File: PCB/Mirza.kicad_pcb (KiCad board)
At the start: 2 copper layers, 74 x 34 mm, 99 parts, among them J1 In, J2 Out, J3 Power, Q1 PMP5201Y, Q10 PMP5201Y, Q11 PMP4201Y, Q12 PMP4201Y, Q13 2SC3324, Q14 2SA1312, Q15 2SA1312, Q16 2SA1312, Q17 2SC3324, Q18 2SC3324, Q19 PMP4201Y, Q2 PMP4201Y, Q20 PMP5201Y, Q21 PMP4201Y, Q22 2SA1312, Q23 2SC3324, Q24 2SC3324, Q25 2SA1312, Q26 D45H11, Q27 D44H11, Q28 PMP5201Y, Q3 2SA1312, Q4 2SC3324, Q5 2SC3324, Q6 2SC3324, Q7 2SA1312, Q8 2SA1312, Q9 PMP5201Y, U1 OPA604

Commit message: Initial public upload
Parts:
- added H3: JLC Tooling Hole, Ariamelon-HolePad:MountingHole_JLC-Tooling, F.Cu at (67.0, 83.0)
- added H4: JLC Tooling Hole, Ariamelon-HolePad:MountingHole_JLC-Tooling, F.Cu at (67.0, 52.0)
- added H5: JLC Tooling Hole, Ariamelon-HolePad:MountingHole_JLC-Tooling, F.Cu at (129.5, 80.0)
- added H6: JLC Tooling Hole, Ariamelon-HolePad:MountingHole_JLC-Tooling, F.Cu at (129.5, 55.0)
- added R32: 1, Resistor_SMD:R_MiniMELF_MMA-0204, F.Cu at (114.8, 61.4)
- added R33: 1, Resistor_SMD:R_MiniMELF_MMA-0204, F.Cu at (114.8, 73.6)
- added R34: 1, Resistor_SMD:R_MiniMELF_MMA-0204, F.Cu at (117.2, 61.4)
- added R35: 1, Resistor_SMD:R_MiniMELF_MMA-0204, F.Cu at (117.2, 73.6)
- C14: renamed from C10; value 1u -> 100n
- C15: renamed from C11; value 1u -> 100n
- C16: renamed from C12; footprint Capacitor_THT:CP_Radial_D6.3mm_P2.50mm -> Ariamelon-Device:CP_Radial_D6.3mm_P2.50mm
- C17: renamed from C13; footprint Capacitor_THT:CP_Radial_D6.3mm_P2.50mm -> Ariamelon-Device:CP_Radial_D6.3mm_P2.50mm
- C18: renamed from C14; footprint Capacitor_THT:CP_Radial_D6.3mm_P2.50mm -> Ariamelon-Device:CP_Radial_D6.3mm_P2.50mm
- C19: renamed from C15; footprint Capacitor_THT:CP_Radial_D6.3mm_P2.50mm -> Ariamelon-Device:CP_Radial_D6.3mm_P2.50mm
- C6: renamed from C19; footprint Capacitor_THT:CP_Radial_D6.3mm_P2.50mm -> Ariamelon-Device:CP_Radial_D6.3mm_P2.50mm
- C7: renamed from C21; footprint Capacitor_THT:CP_Radial_D6.3mm_P2.50mm -> Ariamelon-Device:CP_Radial_D6.3mm_P2.50mm
- C8: renamed from C20; footprint Capacitor_THT:CP_Radial_D6.3mm_P2.50mm -> Ariamelon-Device:CP_Radial_D6.3mm_P2.50mm
- C9: renamed from C18; footprint Capacitor_THT:CP_Radial_D6.3mm_P2.50mm -> Ariamelon-Device:CP_Radial_D6.3mm_P2.50mm
- H1, H2: footprint MountingHole:MountingHole_3.2mm_M3_Pad -> Ariamelon-HolePad:MountingHole_3.2mm_M3_Pad
- Q1, Q10, Q9: value PMP5201Y -> BCM857BS
- Q11, Q19, Q2: value PMP4201Y -> BCM847BS
- Q12: value PMP4201Y -> BCM847BS; footprint Package_TO_SOT_SMD:SOT-363_SC-70-6 -> Ariamelon-Package:SOT-363_SC-70-6
- Q20: renamed from Q28; value PMP5201Y -> BCM857BS
- Q21: renamed from Q20; value PMP5201Y -> BCM857BS
- Q22: renamed from Q21; value PMP4201Y -> BCM847BS
- R11, R14: value 560 -> 220
- R17, R21: value 220 -> 150
- R19, R22, R3, R4: value 100k -> 10k
- R23: renamed from R39; value 100k -> 10k
- R25: renamed from R24; value 100k -> 10k
- R36: renamed from R31; value 0R33 -> 1; footprint Resistor_SMD:R_MELF_MMB-0207 -> Resistor_SMD:R_MiniMELF_MMA-0204
- R37: renamed from R32; value 0R33 -> 1; footprint Resistor_SMD:R_MELF_MMB-0207 -> Resistor_SMD:R_MiniMELF_MMA-0204
- R38: renamed from R33; value 68 -> 150
- R41: renamed from R38; value 100k -> 10k
- U1: value OPA604 -> ADA4522-1
- moved R36 4.55 mm to (119.6, 61.4), turned to -90 degrees
- moved R37 4.55 mm to (119.6, 73.6), turned to -90 degrees
- moved Q7 0.51 mm to (75.7, 79.7), turned to 180 degrees
- moved C13 0.50 mm to (126.6, 67.5), turned to 0 degrees
- moved C16 0.50 mm to (124.3, 61.5)
- moved C17 0.50 mm to (124.3, 71.0)
- moved C18 0.50 mm to (131.3, 61.5)
- moved C19 0.50 mm to (131.3, 71.0)
- moved Q19 0.50 mm to (101.7, 52.6), turned to 180 degrees
- moved Q20 0.50 mm to (101.7, 82.3), turned to 180 degrees
- moved Q6 0.50 mm to (75.7, 55.4), turned to 180 degrees
- moved R38 0.50 mm to (122.4, 67.5), turned to 0 degrees
- moved J2 0.40 mm to (117.9, 68.8)
- moved F1 0.40 mm to (136.7, 60.4), turned to 0 degrees
- moved F2 0.40 mm to (136.7, 74.6), turned to 0 degrees
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- renumbered C6 to C10, C7 to C11, C8 to C12, C9 to C13, C16 to C20, C17 to C21, Q22 to Q23, Q23 to Q24, Q24 to Q25, Q25 to Q26, Q26 to Q27, Q27 to Q28, R23 to R24, R25 to R26, R26 to R27, R27 to R28, R28 to R29, R29 to R30, R30 to R31, R34 to R39, R35 to R40, R36 to R42, R37 to R43
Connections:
- C11 pad 1: Net-(Q20B-C2) -> Net-(Q21A-C1)
- C12 pad 1: Net-(Q25-C) (its old number) -> Net-(Q26-C)
- C12 pad 2: Net-(Q21B-C2) -> Net-(Q22A-C1)
- C13 pad 1: GND -> Net-(C13-Pad1)
- C13 pad 2: Net-(C9-Pad2) -> GND
- C14 pad 1: GND -> Net-(U1-+)
- C14 pad 2: Net-(U1-+) -> GND
- C15 pad 1: Net-(U1--) -> Net-(C15-Pad1)
- C15 pad 2: Net-(C11-Pad2) -> Net-(U1--)
- C21 pad 1: VEE -> GND
- C21 pad 2: GND -> VEE
- C3 pad 1: Net-(C3-Pad1) -> Net-(Q11A-B1)
- C3 pad 2: Net-(Q11A-B1) -> Net-(C3-Pad2)
- C5 pad 1: Net-(C3-Pad1) -> Net-(C3-Pad2)
- C7 pad 2: Net-(Q28B-B2) -> Net-(Q20A-B1)
- C9 pad 1: Net-(Q19B-B2) -> Net-(Q19A-B1)
- F1 pad 1: Net-(J3-Pin_1) -> +18V
- F1 pad 2: +18V -> Net-(J3-Pin_1)
- F2 pad 1: Net-(J3-Pin_4) -> -18V
- F2 pad 2: -18V -> Net-(J3-Pin_4)
- Q10 pad 3: Net-(Q10B-C2) -> Net-(Q10A-B1)
- Q10 pad 6: Net-(Q10A-B1) -> Net-(Q10A-C1)
- Q11 pad 3: Net-(Q11B-C2) -> Net-(Q11A-B1)
- Q11 pad 6: Net-(Q11A-B1) -> Net-(Q11A-C1)
- Q12 pad 2: Net-(Q11B-E2) -> Net-(Q11A-E1)
- Q12 pad 5: Net-(Q11B-E2) -> Net-(Q11A-E1)
- Q13 pad 2: Net-(Q10B-C2) -> Net-(Q10A-C1)
- Q14 pad 2: Net-(Q11B-C2) -> Net-(Q11A-C1)
- Q15 pad 3: Net-(Q10B-C2) -> Net-(Q10A-C1)
- Q18 pad 3: Net-(Q11B-C2) -> Net-(Q11A-C1)
- Q19 pad 1: VCC -> Net-(Q19A-E1)
- Q19 pad 4: Net-(Q19A-B1) -> VCC
- Q19 pad 5: Net-(Q19B-B2) -> Net-(Q19A-E1)
- Q20 pad 1: VEE -> Net-(Q20A-E1)
- Q20 pad 2: Net-(Q28A-B1) -> Net-(Q20A-B1)
- Q20 pad 4: Net-(Q28A-B1) -> VEE
- Q20 pad 5: Net-(Q28B-B2) -> Net-(Q20A-E1)
- Q21 pad 1: +18V -> Net-(Q21A-E1)
- Q21 pad 2: Net-(Q20A-B1) -> Net-(Q21A-B1)
- Q21 pad 3: Net-(Q20B-C2) -> Net-(Q21A-B1)
- Q21 pad 4: Net-(Q20A-B1) -> +18V
- Q21 pad 5: Net-(Q20A-C1) -> Net-(Q21A-E1)
- Q21 pad 6: Net-(Q20A-C1) -> Net-(Q21A-C1)
- Q22 pad 1: -18V -> Net-(Q22A-E1)
- Q22 pad 2: Net-(Q21A-B1) -> Net-(Q22A-B1)
- Q22 pad 3: Net-(Q21B-C2) -> Net-(Q22A-B1)
- Q22 pad 4: Net-(Q21A-B1) -> -18V
- Q22 pad 5: Net-(Q21A-C1) -> Net-(Q22A-E1)
- Q22 pad 6: Net-(Q21A-C1) -> Net-(Q22A-C1)
- Q23 pad 2: Net-(Q22-C) -> Net-(Q23-C)
- Q24 pad 2: Net-(Q23-C) -> Net-(Q24-C)
- Q24 pad 3: Net-(Q23-E) (its old number) -> Net-(Q24-E)
- Q25 pad 1: Net-(Q20B-C2) -> Net-(Q21A-C1)
- Q25 pad 3: Net-(Q23-C) -> Net-(Q24-C)
- Q26 pad 1: Net-(Q21B-C2) -> Net-(Q22A-C1)
- Q26 pad 2: Net-(Q25-C) (its old number) -> Net-(Q26-C)
- Q26 pad 3: Net-(Q22-C) -> Net-(Q23-C)
- Q27 pad 2: Net-(Q23-C) -> Net-(Q24-C)
- Q28 pad 1: Net-(Q25-C) (its old number) -> Net-(Q26-C)
- Q28 pad 2: Net-(Q22-C) -> Net-(Q23-C)
- Q9 pad 2: Net-(Q10B-E2) -> Net-(Q10A-E1)
- Q9 pad 3: Net-(Q10A-E1) -> Net-(Q10B-E2)
- Q9 pad 5: Net-(Q10B-E2) -> Net-(Q10A-E1)
- Q9 pad 6: Net-(Q10B-E2) -> Net-(Q10A-E1)
- R1 pad 1: Net-(C1-Pad2) -> Net-(J1-Pin_2)
- R1 pad 2: Net-(J1-Pin_2) -> Net-(C1-Pad2)
- R10 pad 1: Net-(Q2A-B1) -> VEE
- R10 pad 2: VEE -> Net-(Q2A-B1)
- R11 pad 1: VCC -> Net-(Q9B-E2)
- R11 pad 2: Net-(Q9B-E2) -> VCC
- R12 pad 1: Amp_FB -> Net-(Q4-C)
- R12 pad 2: Net-(Q4-C) -> Amp_FB
- R13 pad 1: Net-(Q3-C) -> Amp_FB
- R13 pad 2: Amp_FB -> Net-(Q3-C)
- R14 pad 1: Net-(Q12B-E2) -> VEE
- R14 pad 2: VEE -> Net-(Q12A-E1)
- R15 pad 1: Amp_Out -> Net-(C2-Pad2)
- R15 pad 2: Net-(C2-Pad2) -> Amp_Out
- R16 pad 1: Net-(C3-Pad1) -> Net-(C3-Pad2)
- R17 pad 1: Net-(Q9A-E1) -> VCC
- R17 pad 2: VCC -> Net-(Q9A-E1)
- R19 pad 1: Net-(Q17-B) -> Net-(Q16-B)
- R19 pad 2: Net-(Q16-B) -> Net-(Q17-B)
- R21 pad 2: Net-(Q12A-E1) -> Net-(Q12B-E2)
- R22 pad 1: +18V -> Net-(Q19A-B1)
- R22 pad 2: Net-(Q19B-B2) -> +18V
- R23 pad 1: -18V -> Net-(Q20A-B1)
- R23 pad 2: Net-(Q28B-B2) -> -18V
- R25 pad 1: Net-(Q21A-C1) -> Net-(Q21A-B1)
- R25 pad 2: Net-(Q20A-C1) -> Net-(Q22A-B1)
- R26 pad 1: Net-(R25-Pad1) -> Net-(Q21A-E1)
- R26 pad 2: Net-(Q20A-B1) -> Net-(R26-Pad2)
- R27 pad 2: Net-(Q20B-C2) -> Net-(Q21A-C1)
- R28 pad 1: Net-(Q21B-C2) -> Net-(Q24-E)
- R28 pad 2: Net-(Q23-E) (its old number) -> Net-(Q22A-C1)
- R29 pad 1: Net-(Q21A-B1) -> Net-(Q22A-E1)
- R31 pad 1: -18V -> Net-(Q26-C)
- R31 pad 2: Net-(Q25-C) (its old number) -> -18V
- R36 pad 1: Amp_Out -> Net-(Q24-C)
- R36 pad 2: Net-(Q23-C) -> Amp_Out
- R37 pad 1: Net-(Q22-C) -> Amp_Out
- R37 pad 2: Amp_Out -> Net-(Q23-C)
- R38 pad 1: Net-(C9-Pad2) -> Amp_Out
- R38 pad 2: Amp_Out -> Net-(C13-Pad1)
- R39 pad 1: GND -> Net-(U1--)
- R39 pad 2: Net-(U1--) -> GND
- R4 pad 1: Net-(Q2A-C1) -> Net-(Q1A-C1)
- R4 pad 2: Net-(Q1A-C1) -> Net-(Q2A-C1)
- R41 pad 1: Net-(C11-Pad2) -> Amp_FB
- R41 pad 2: Amp_FB -> Net-(C15-Pad1)
- R43 pad 1: Amp_FB -> GND
- R43 pad 2: GND -> Amp_FB
- R5 pad 1: VCC -> Net-(Q1A-B1)
- R5 pad 2: Net-(Q1A-B1) -> VCC
- R8 pad 1: Net-(Q7-B) -> Net-(Q4-E)
- R8 pad 2: Net-(Q4-E) -> Net-(Q7-B)
- R9 pad 1: Net-(Q2B-C2) -> Net-(Q7-B)
- R9 pad 2: Net-(Q7-B) -> Net-(Q2B-C2)
- RV1 pad 3: Net-(R25-Pad1) -> Net-(R26-Pad2)
- U1 pad 6: Net-(C11-Pad2) -> Net-(C15-Pad1)
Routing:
- net Net-(Q26-C): track 0.00 -> 21.6 mm, vias 0 -> 1
- net Net-(Q25-C) (its old number): track 21.6 -> 0.00 mm, vias 1 -> 0
- net Net-(Q22-C): track 19.7 -> 0.00 mm
- net Net-(Q24-C): track 0.00 -> 19.2 mm
- net Net-(Q10B-C2): track 12.5 -> 0.00 mm
- net Net-(Q10A-C1): track 0.00 -> 12.5 mm
- net Net-(Q11B-C2): track 12.4 -> 0.00 mm
- net Net-(Q11A-C1): track 0.00 -> 12.4 mm
- net Net-(C15-Pad1): track 0.00 -> 7.81 mm
- net Net-(C11-Pad2): track 7.81 -> 0.00 mm
- net Net-(Q20A-C1): track 7.81 -> 0.00 mm, vias 2 -> 0
- net Net-(Q22A-B1): track 0.00 -> 7.69 mm, vias 0 -> 2
- net Net-(Q22A-C1): track 0.00 -> 7.29 mm
- net Net-(Q21B-C2): track 7.29 -> 0.00 mm
- net Net-(Q23-C): track 22.7 -> 15.6 mm
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- added copper zone on F.Cu, net Net-(C13-Pad1)
- added copper zone on F.Cu, net Net-(Q19A-B1)
- added copper zone on F.Cu, net Net-(Q20A-B1)
- added copper zone on F.Cu, net Net-(Q24-C)
- removed copper zone on F.Cu, net Net-(C9-Pad2)
- removed copper zone on F.Cu, net Net-(Q19B-B2)
- removed copper zone on F.Cu, net Net-(Q22-C)
- removed copper zone on F.Cu, net Net-(Q28B-B2)

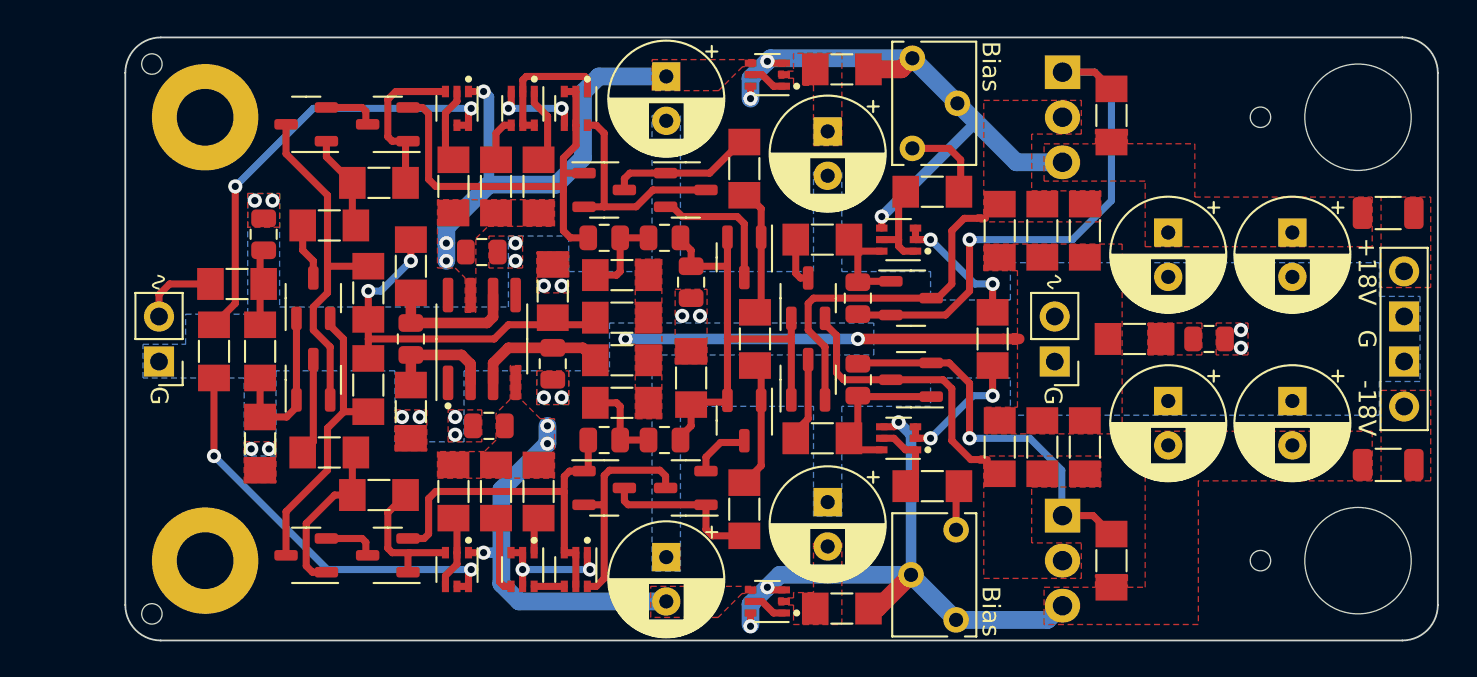
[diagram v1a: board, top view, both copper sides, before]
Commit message: 17/09/2023 update
Repositioning of parts. Added interactive BOM. Changed some values. Removed PTC fuses. Lengthened board to add JST XH connectors.
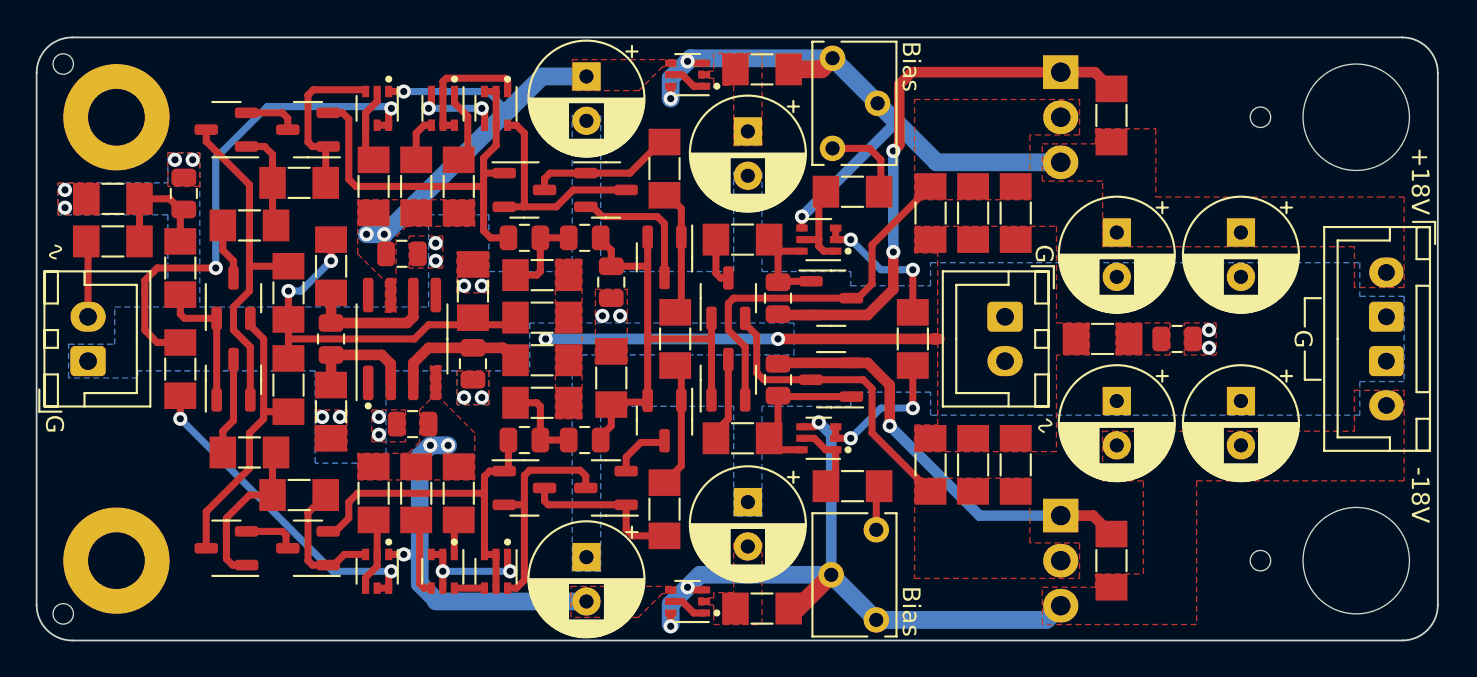
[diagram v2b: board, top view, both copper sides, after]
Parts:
- removed F1, F2: 500mA, Ariamelon-Device:Fuse_1206_3216Metric
- C13: value 100p -> 10n
- C14, C15, C20, C21: value 100n -> 1u
- J1, J2: footprint Connector_PinHeader_2.54mm:PinHeader_1x02_P2.54mm_Vertical -> Connector_JST:JST_XH_B2B-XH-A_1x02_P2.50mm_Vertical
- J3: footprint Ariamelon-Header:PinHeader_1x04_P2.54mm_Vertical_MiddleGND -> Ariamelon-Connector:JST_XH_B4B-XH-A_1x04_P2.50mm_Vertical_MiddleGND
- R11, R14: value 220 -> 560
- R17, R21: value 150 -> 220
- R19, R41: value 10k -> 100k
- R32, R33, R34, R35, R36, R37: value 1 -> 1R5
- R38: value 150 -> 68
- moved R2 16.1 mm to (64.8, 59.6), turned to 180 degrees
- moved R36 8.76 mm to (110.9, 60.4)
- moved R37 8.76 mm to (110.9, 74.6)
- moved R1 7.40 mm to (64.8, 62.0)
- moved R3 6.51 mm to (68.6, 63.5)
- moved C1 5.05 mm to (68.8, 59.3)
- moved H1 5.00 mm to (65.0, 80.0)
- moved H2 5.00 mm to (65.0, 55.0)
- moved H3 5.00 mm to (62.0, 83.0)
- moved H4 5.00 mm to (62.0, 52.0)
- moved Q7 4.52 mm to (71.2, 79.3)
- moved Q8 4.52 mm to (75.8, 79.3)
- moved Q5 4.51 mm to (75.8, 55.7)
- moved Q6 4.51 mm to (71.2, 55.7)
- moved Q12 4.50 mm to (83.4, 80.6)
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- renumbered R3 to R2, R2 to R3
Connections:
- J3 pad 1: Net-(J3-Pin_1) -> +18V
- J3 pad 4: Net-(J3-Pin_4) -> -18V
- R2 pad 1: Net-(Q3-B) -> Net-(C1-Pad2)
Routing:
- net Net-(Q2A-C1): track 23.2 -> 18.4 mm
- net -18V: track 35.6 -> 40.0 mm
- net +18V: track 34.2 -> 38.6 mm
- net Net-(C1-Pad2): track 3.70 -> 7.03 mm
- net Net-(Q1A-C1): track 25.1 -> 28.3 mm
- net VCC: track 26.2 -> 23.3 mm
- net Net-(Q26-C): track 21.6 -> 24.2 mm
- net Net-(Q23-C): track 15.6 -> 17.4 mm
- net Net-(Q24-C): track 19.2 -> 20.9 mm
- net Net-(Q3-B): track 9.08 -> 7.85 mm
- net Net-(Q11A-B1): track 20.7 -> 19.7 mm
- net VEE: track 21.4 -> 20.5 mm
- net Net-(Q10A-B1): track 24.5 -> 23.9 mm
- net Net-(Q25-C): track 31.3 -> 31.4 mm, vias 1 -> 2
- removed copper zone on F.Cu, net Net-(J3-Pin_1)
- removed copper zone on F.Cu, net Net-(J3-Pin_4)
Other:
- board size 74 x 34 mm -> 79 x 34 mm
